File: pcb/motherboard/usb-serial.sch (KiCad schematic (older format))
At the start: 22 parts, among them J13 USB-LED, J2 USB-MINI-B, J4 ICSP-USB, U3 ATMEGA8U2-AU, Y1 16.00 MHz

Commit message: Adjusted page size for motherboard schematic
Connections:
- net labels added: URESET, URXD, UTXD
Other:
- moved on the sheet: C1, C11, C2, C3, C4, C5, C6, J13, J2, J4, R1, R2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

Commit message: Updated PCB design
+ Completed daughterboard PCB layout.
* Corrected soldermask clerance on front panel pcb.
- Removed input resistor on DIN for RGB lamp board.
* Modified PCB layout for PSU board.
* Updated gerber files.
* Updated schematics pdf, BOM.
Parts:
- removed C3, C6: 100nF, smt:C-0603, symbol passive:CAP
- added C28, C29: 100nF, smt:C-0603, symbol passive:CAP
- added D2: CD1206-S01575, smt:D-1206, symbol passive:DIODE
- added R19, R33: 1k, smt:R-0603, symbol passive:RESISTOR
- added R24, R26: 0, smt:R-0805, symbol passive:RESISTOR
- added R25: N/A, smt:R-0805, symbol passive:RESISTOR
- added R27, R30: 10k, smt:R-0603, symbol passive:RESISTOR
- added R28, R29, R32: N/A, smt:R-0603, symbol passive:RESISTOR
- added R31: 100k, smt:R-0603, symbol passive:RESISTOR
- added U8: 74LVC2G126DC, smt-sop:VSSOP8, symbol ic-logic:74?2G126
- added U9: 74AHC1G126SE-7, smt-sot:SOT-353, symbol ic-logic:74?1G126
- F1: footprint smt:FER-0805 -> smt:FER-1206; Part - -> 1206L050/15YR
- J13: footprint conn-wire-pads:WP-50mil-1x02 -> conn-wire-pads:WP-50mil-1x03; symbol connectors:HEADER-1x02 -> connectors:HEADER-1x03
- J4: value ICSP-USB -> ICSP-0
- L1: Part - -> BLM21BB050SZ1D
- R1: value 1k -> 10k
- R2: value 1k -> 100k
- U3: value ATMEGA8U2-AU -> ATMEGA16U2-AU
- Y1: footprint crystals:HC49USX -> crystals:smt-CSM-3X-7x4mm
- Z1, Z2: value PGB1010603 -> CG0603MLC-05E; Part - -> CG0603MLC-05E
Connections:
- net labels added: RESET-M, SUP_UVCC
- net labels removed: URESET
- wire segments 97 -> 159
- no-connect marks 14 -> 15
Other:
- moved on the sheet: C1, C11, C2, C4, C5, J2, J4, R3, R4, R5, R7, U3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

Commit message: Fix: Wrong footprint for R20-22 and C14
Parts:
- J4: value ICSP-0 -> ICSP
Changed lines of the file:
@@
 P 9650 1950
 F 0 "J4" H 9550 2150 60  0000 L BNB
-F 1 "ICSP-0" H 9500 1750 40  0000 L TNN
+F 1 "ICSP" H 9500 1750 40  0000 L TNN
 F 2 "conn-header:HDR-M-2x03" H 9650 750 60  0001 C CNN
 F 3 "" H 9650 750 60  0001 C CNN

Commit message: Corrected solder mask clearance
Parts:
- removed C28, C29: 100nF, smt:C-0603, symbol passive:CAP
- removed F1: 500mA, smt:FER-1206, symbol passive:FUSE
- removed J13: USB-LED, conn-wire-pads:WP-50mil-1x03, symbol connectors:HEADER-1x03
- removed L1: BLM21, smt:FER-0805, symbol passive:INDUCTOR
- removed R19, R33: 1k, smt:R-0603, symbol passive:RESISTOR
- removed R24, R26: 0, smt:R-0805, symbol passive:RESISTOR
- removed R25: N/A, smt:R-0805, symbol passive:RESISTOR
- removed R27, R30: 10k, smt:R-0603, symbol passive:RESISTOR
- removed R29: N/A, smt:R-0603, symbol passive:RESISTOR
- removed R31: 100k, smt:R-0603, symbol passive:RESISTOR
- removed U8: 74LVC2G126DC, smt-sop:VSSOP8, symbol ic-logic:74?2G126
- removed U9: 74AHC1G126SE-7, smt-sot:SOT-353, symbol ic-logic:74?1G126
- removed Z1, Z2: CG0603MLC-05E, smt:FER-0603, symbol passive:SUPRESSOR
- added DA1: SR05, smt-sot:SOT-143, symbol passive:SR05
- added F1: 500mA, smt:R-1206, symbol passive:PTC
- added J13: USB-LED, conn-wire-pads:WP-50mil-1x04, symbol connectors:HEADER-1x04
- added Q1: MMST3904, smt-sot:SOT23, symbol transistor:MMST3904
- R19: renamed from R32; value N/A -> 1k
- R2: value 100k -> 10k
- R24: renamed from R28; value N/A -> 1k
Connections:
- net labels added: VUSB-DET
- net labels removed: RESET-M, SUP_UVCC, USHLD
- wire segments 159 -> 111
- no-connect marks 15 -> 13
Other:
- moved on the sheet: C1, C11, C2, C4, C5, D2, J2, J4, R19, R24, R3, R4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

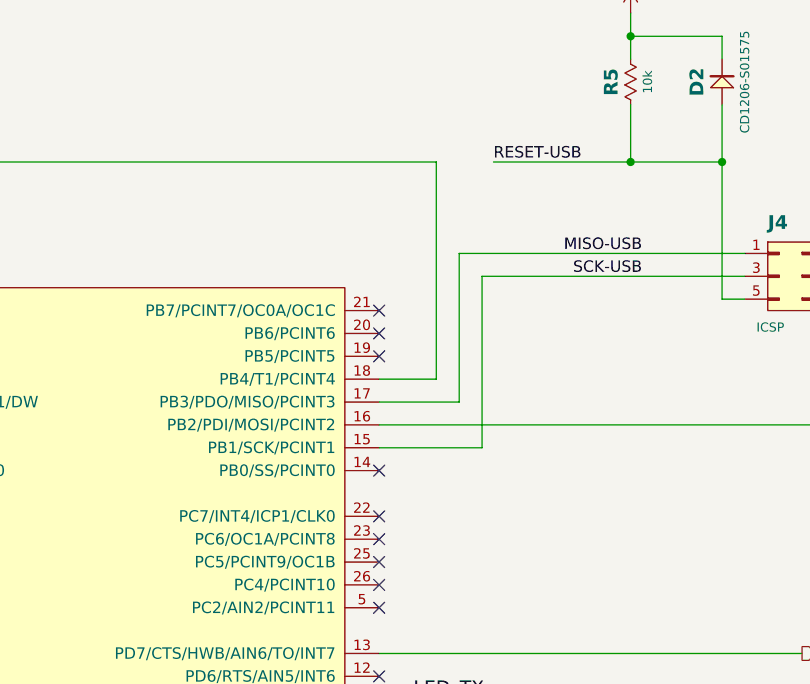
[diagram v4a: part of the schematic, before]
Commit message: Changed pin for VUSB detection on U3
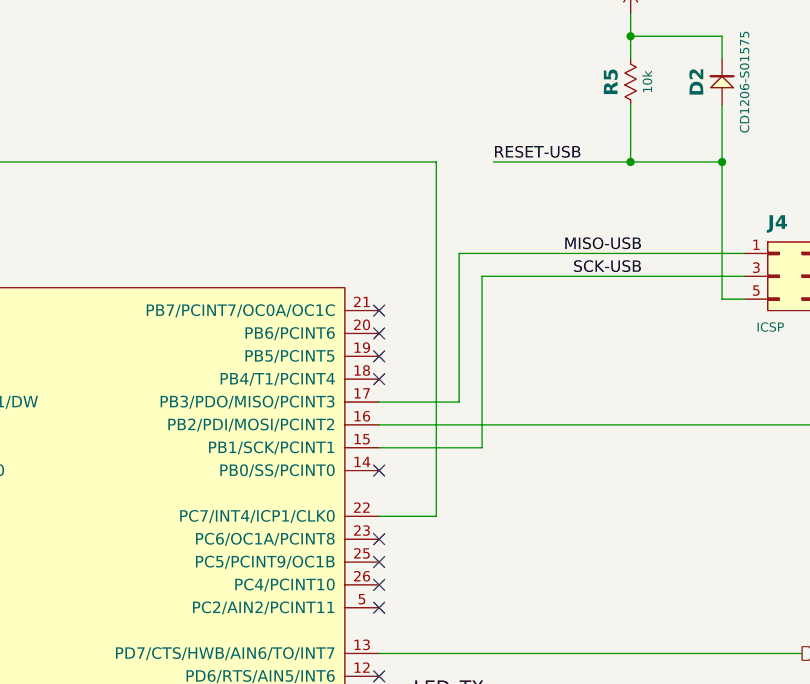
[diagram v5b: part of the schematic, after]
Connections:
- net VUSB-DET: now also U3.22 (PC7/INT4/ICP1/CLK0); no longer U3.18 (PB4/T1/PCINT4)
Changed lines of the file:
@@
 NoConn ~ 7700 3400
 NoConn ~ 7700 3900
-NoConn ~ 7700 4100
+NoConn ~ 7700 3500
 NoConn ~ 7700 4200
 NoConn ~ 7700 4300
@@
 VUSB-DET
 Wire Wire Line
-	7700 3500 7950 3500
-Wire Wire Line
-	7950 3500 7950 2550
-Wire Wire Line
 	3200 2550 7950 2550
 Text Label 7850 5100 0    60   ~ 0
@@
 Wire Wire Line
 	8800 6400 8800 6550
+Wire Wire Line
+	7950 4100 7700 4100
+Wire Wire Line
+	7950 2550 7950 4100
 $EndSCHEMATC
